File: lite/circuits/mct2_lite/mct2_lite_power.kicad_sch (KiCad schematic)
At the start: 136 parts

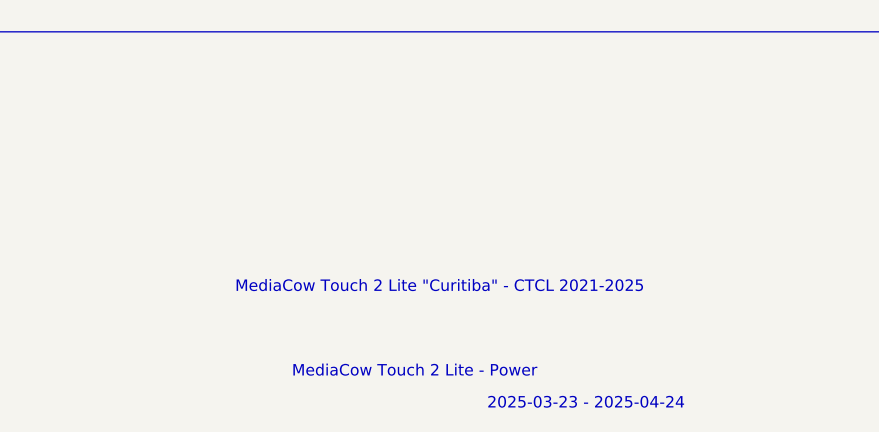
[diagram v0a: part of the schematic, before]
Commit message: 20250426-1 Remove current codename
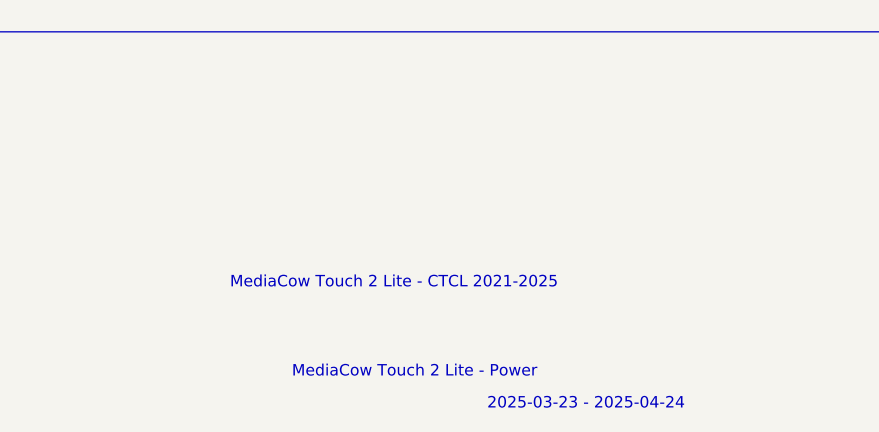
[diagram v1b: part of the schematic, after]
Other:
- note added: "MediaCow Touch 2 Lite - CTCL 2021-2025"
- note removed: "MediaCow Touch 2 Lite "Curitiba" - CTCL 2021-2025"
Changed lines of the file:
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@@
 		)
 	)
-	(text "MediaCow Touch 2 Lite \"Curitiba\" - CTCL 2021-2025"
+	(text "MediaCow Touch 2 Lite - CTCL 2021-2025"
 		(exclude_from_sim no)
-		(at 501.396 390.398 0)
+		(at 496.316 389.89 0)
 		(effects
 			(font

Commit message: 20250504-1
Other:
- note added: "2025-03-23 - 2025-04-29"
- note added: "MediaCow Touch 2 Lite "Curitiba" - CTCL 2021-2025"
- note removed: "2025-03-23 - 2025-04-24"
- note removed: "MediaCow Touch 2 Lite - CTCL 2021-2025"
- moved on the sheet: C?, D?, J?, L?, Q?, R?, U?

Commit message: 20250509-1
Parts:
- added C? (x2): 10uF, symbol Device:C_Small
- added C?: 470nF, symbol Device:C_Small
- added C? (x3): 1uF, symbol Device:C_Small
- added C?: 33pF, symbol Device:C_Small
- added C?: 1.2nF, symbol Device:C_Small
- added C? (x2): 100pF, symbol Device:C_Small
- added C?: 3.3uF, symbol Device:C_Small
- added C? (x2): 47nF, symbol Device:C_Small
- added C?: 15pF, symbol Device:C_Small
- added C?: 3.3nF, symbol Device:C_Small
- added C? (x2): 33nF, symbol Device:C_Small
- added C?: 33uF, symbol Device:C_Small
- added C? (x2): 100nF, symbol Device:C_Small
- added C?: 1nF, symbol Device:C_Small
- added L?: 2.2uH, symbol Device:L
- added Q?: BSC084P03NS3G, Package_SON:Infineon_PG-TDSON-8_6.15x5.15mm, symbol mediacow:BSC084P03NS3G
- added Q? (x4): IAUCN04S7L028, mediacow:Infineon_PG-TDSON-8-33, symbol mediacow:IAUCN04S7L028
- added R? (x2): 4.99, symbol Device:R_Small
- added R? (x5): 10K, symbol Device:R_Small
- added R? (x2): 10m, symbol Device:R_Small
- added R?: 300K, symbol Device:R_Small
- added R?: 1, symbol Device:R_Small
- added R?: 30K, symbol Device:R_Small
- added R?: 250K, symbol Device:R_Small
- added R? (x3): 10, symbol Device:R_Small
- added R?: 16.9K, symbol Device:R_Small
- added R?: 50, symbol Device:R_Small
- added R?: 137K, symbol Device:R_Small
- added R?: 380K, symbol Device:R_Small
- added R?: 350K, symbol Device:R_Small
- added R?: 2M, symbol Device:R_Small
- added R?: 220K, symbol Device:R_Small
- added R?: 2.2, symbol Device:R_Small
- Q? (x4): footprint (none) -> Package_TO_SOT_SMD:SOT-23
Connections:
- net GND: now also U?.27 (PGND), C?.1, C?.2, C?.2, C?.2, C?.2, C?.2, C?.2, C?.2, C?.2, C?.2, C?.2, C?.2, C?.2, C?.2, C?.2, C?.2, C?.2, C?.2, Q?.1 (S), Q?.1 (S), R?.2, R?.2, R?.2, R?.2
- net TCP0_VBUS: no longer Q?.2 (S), Q?.3 (S)
- net TCP1_VBUS: no longer Q?.2 (S), Q?.3 (S)
- net VBUS: now also C?.1, R?.1, R?.1, R?.1, R?.1
- net at C?.1, C?.1, C?.1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: no longer Q?.2 (S), Q?.3 (S) (x2)
- net at C?.2, C?.2, C?.2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: now also Q?.2 (G), Q?.2 (G); no longer Q?.4 (G), Q?.4 (G) (x2)
- net at U?.1 (VBUS): now also C?.1, R?.2
- net at U?.10 (PSYS): now also R?.1
- net SOM_PROCHOT: now reaches U?.11 (~{PROCHOT})
- net SOM_PROCHOT: now also R?.2
- net EC_BM_I2C_SDA: now reaches U?.12 (SDA)
- net EC_BM_I2C_SDA: now also R?.2
- net EC_BM_I2C_SCL: now reaches U?.13 (SCL)
- net EC_BM_I2C_SCL: now also R?.2
- net at U?.14 (CMPIN): now also R?.1, R?.2
- net BM_CMPOUT: now reaches U?.15 (CMPOUT)
- net BM_CMPOUT: now also R?.2
- net at U?.16 (COMP1): now also C?.1, R?.2
- net at U?.17 (COMP2): now also C?.1, R?.2
- net at U?.18 (CELL_BATPRESZ): now also R?.1, R?.2
- net at U?.19 (SRN): now also R?.2
- net at U?.2 (ACN): now also C?.1, R?.2
- net at U?.20 (SRP): now also R?.2
- net at U?.21 (~{BATDRV}): now also Q?.4 (G)
- net at U?.22 (VSYS): now also Q?.3 (D), Q?.5 (D), Q?.6 (D), Q?.7 (D), Q?.8 (D)
- net at U?.23 (SW2): now also C?.1, L?.2, Q?.1 (S), Q?.3 (D)
- net at U?.24 (HIDRV2): now also Q?.2 (G)
- net at U?.25 (BTST2): now also C?.2
- net at U?.26 (LODRV2): now also Q?.2 (G)
- net BM_REGN: now reaches U?.28 (REGN)
- net BM_REGN: now also C?.1, R?.1
- net at U?.29 (LODRV1): now also Q?.2 (G)
- net at U?.3 (ACP): now also C?.1, R?.2
- net at U?.30 (BTST1): now also C?.2
- net at U?.31 (HIDRV1): now also Q?.2 (G)
- net at U?.32 (SW1): now also C?.1, L?.1, Q?.1 (S), Q?.3 (D)
- net BM_CHRGOK: now reaches U?.4 (CHRG_OK)
- net BM_CHRGOK: now also R?.2
- net BM_OTG_VAP_FRS: now reaches U?.5 (OTG/VAP/FRS)
- net at U?.6 (ILIM_HIZ): now also R?.1, R?.1
- net at U?.7 (VDDA): now also C?.2, R?.2, R?.2
- net at U?.8 (IADPT): now also C?.1, R?.1
- net at U?.9 (IBAT): now also C?.1
- new net: C?.1, C?.1, C?.2, R?.1, R?.2
- new net: C?.1, C?.1, Q?.3 (D), R?.1, R?.2
- new net: C?.1, C?.1, Q?.1 (S), Q?.2 (S), Q?.3 (S), R?.1, R?.1
- new net: C?.1, Q?.3 (D), Q?.3 (D), R?.1, R?.1 (x2)
- new net: C?.1, R?.1 (x2)
- new net: C?.1, R?.2
- new net BM_1V05: R?.1
- new net BM_VDDA: R?.1
- new net EC_IOVDD: R?.1, R?.1, R?.1, R?.1
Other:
- note added: "Battery Charge Controller"
- note added: "SoM Load Switch"
- note added: "TCP Controller"
- note removed: "2025-03-23 - 2025-04-29"
- note removed: "MediaCow Touch 2 Lite "Curitiba" - CTCL 2021-2025"
- note removed: "MediaCow Touch 2 Lite - Power"
- company: (none) -> CTCL 2021-2025
- title: (none) -> MediaCow Touch 2 "Curitiba" - Power
- moved on the sheet: C?, D?, R?, U?

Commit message: 20250524-1
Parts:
- removed C?: C_Small, symbol Device:C_Small
- removed D?: TBD, symbol Device:D_Zener_Small
- removed R?: 560K, symbol Device:R_Small
- removed R?: 4.7K, symbol Device:R_Small
- removed R?: 1.2K, symbol Device:R_Small
- added C? (x14): 10uF, Capacitor_SMD:C_1206_3216Metric, symbol Device:C_Small
- added C?: 100nF, Capacitor_SMD:C_0603_1608Metric, symbol Device:C_Small
- added C? (x4): 1uF, Capacitor_SMD:C_0805_2012Metric, symbol Device:C_Small
- added C? (x2): 22uF, Capacitor_Tantalum_SMD:CP_EIA-3528-15_AVX-H, symbol Device:C_Small
- added C? (x5): 22uF, Capacitor_SMD:C_2220_5750Metric, symbol Device:C_Small
- added L?: 10uH, symbol Device:L_Small
- added R?: 47K, Resistor_SMD:R_0603_1608Metric, symbol Device:R_Small
- added R?: 100K, Resistor_SMD:R_0603_1608Metric, symbol Device:R_Small
- added R?: 22.1K, Resistor_SMD:R_0603_1608Metric, symbol Device:R_Small
- added U?: TPS560430, Package_TO_SOT_SMD:SOT-23-6, symbol mediacow:TPS560430
- added U?: TCR3UF105A, Package_TO_SOT_SMD:SC-74A-5_1.55x2.9mm_P0.95mm, symbol mediacow:TCR3UF105A
- C? (x6): footprint (none) -> Capacitor_SMD:C_1206_3216Metric
- C? (x44): footprint (none) -> Capacitor_SMD:C_0603_1608Metric
- C? (x9): footprint (none) -> Capacitor_SMD:C_0805_2012Metric
- C? (x4): footprint (none) -> Capacitor_SMD:C_2220_5750Metric
- C?: footprint (none) -> Capacitor_Tantalum_SMD:CP_EIA-7343-30_AVX-N
- L? (x2): value 4.7uF -> 4.7uH
- R? (x62): footprint (none) -> Resistor_SMD:R_0603_1608Metric
- R? (x2): footprint (none) -> Resistor_SMD:R_1206_3216Metric
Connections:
- net VSYS_SW_DEN is gone; now on net GND: R?.2
- net BM_1V05: now also C?.2, U?.5 (VOUT)
- net GND: now also U?.44 (HRESET), C?.1, C?.1, C?.1, C?.1, C?.1, C?.2, C?.2, C?.2, C?.2, C?.2, C?.2, C?.2, C?.2, C?.2, C?.2, C?.2, C?.2, C?.2, C?.2, C?.2, C?.2, C?.2, C?.2, C?.2, C?.2, R?.1, R?.2, U?.2 (GND), U?.2 (GND)
- net TCP0_PPHV: now also C?.1
- net TCP0_VBUS: now also C?.1
- net TCP1_PPHV: now also C?.1
- net TCP1_VBUS: now also C?.1
- net TCP_LDO_1V8: now also C?.2
- net TCP_LDO_3V3: now also C?.2
- net TCP_PP_5V: now also C?.1, C?.1
- net VBUS: now also C?.1, C?.1, C?.1, C?.1
- net VSYS: now also Q?.3 (D), Q?.5 (D), Q?.6 (D), Q?.7 (D), Q?.8 (D), U?.22 (VSYS), C?.1, C?.1, C?.1, C?.1, C?.1, C?.1, C?.1, C?.1, C?.1, U?.4 (EN), U?.5 (VIN)
- net VBAT: now reaches C?.1, C?.1, C?.2, R?.1, R?.2
- net at U?.4 (IS): now also R?.2
- net TCP0_HPD: now reaches U?.30 (HPD1_(GPIO3))
- net TCP1_HPD: now reaches U?.31 (HPD2_(GPIO4))
- net TCP_VIN_3V3: now reaches U?.5 (VIN_3V3)
- net TCP_VIN_3V3: now also C?.1
- net SOM_VSYS renamed VSYS_SOM
- new net: C?.1, L?.1, U?.6 (SW)
- new net: C?.2, U?.1 (CB)
- new net: C?.2, C?.2, L?.2, R?.1, U?.1 (VIN), U?.3 (CONTROL)
- new net: R?.1, R?.2, U?.3 (FB)
- no-connect marks 0 -> 15
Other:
- moved on the sheet: C?, D?, J?, L?, Q?, R?, U?

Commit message: 20250529-1
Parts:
- gave numbers to parts that had none: 214
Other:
- note added: "TCP Status LED"
- moved on the sheet: C51, C54, C60, D1, R24, U7
